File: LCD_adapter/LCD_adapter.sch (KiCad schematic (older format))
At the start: 3 parts, among them U1 RC1602A

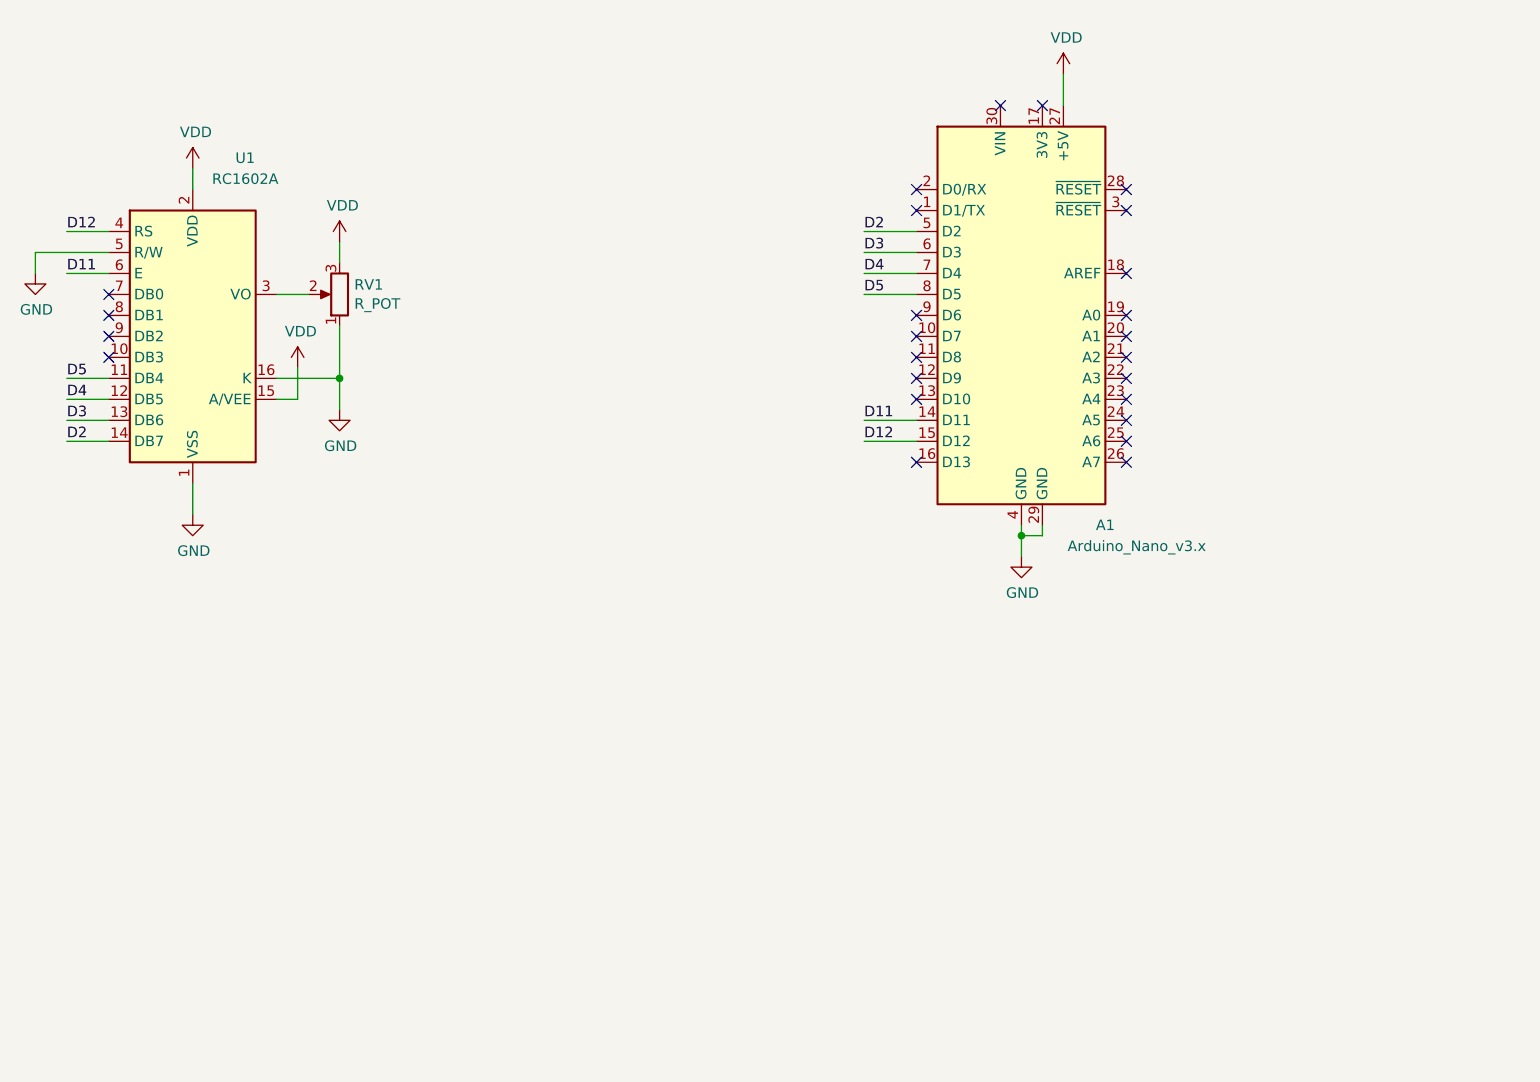
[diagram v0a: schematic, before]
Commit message: bluetooth module v0 - updated to include the bluetooth module and buttons for control
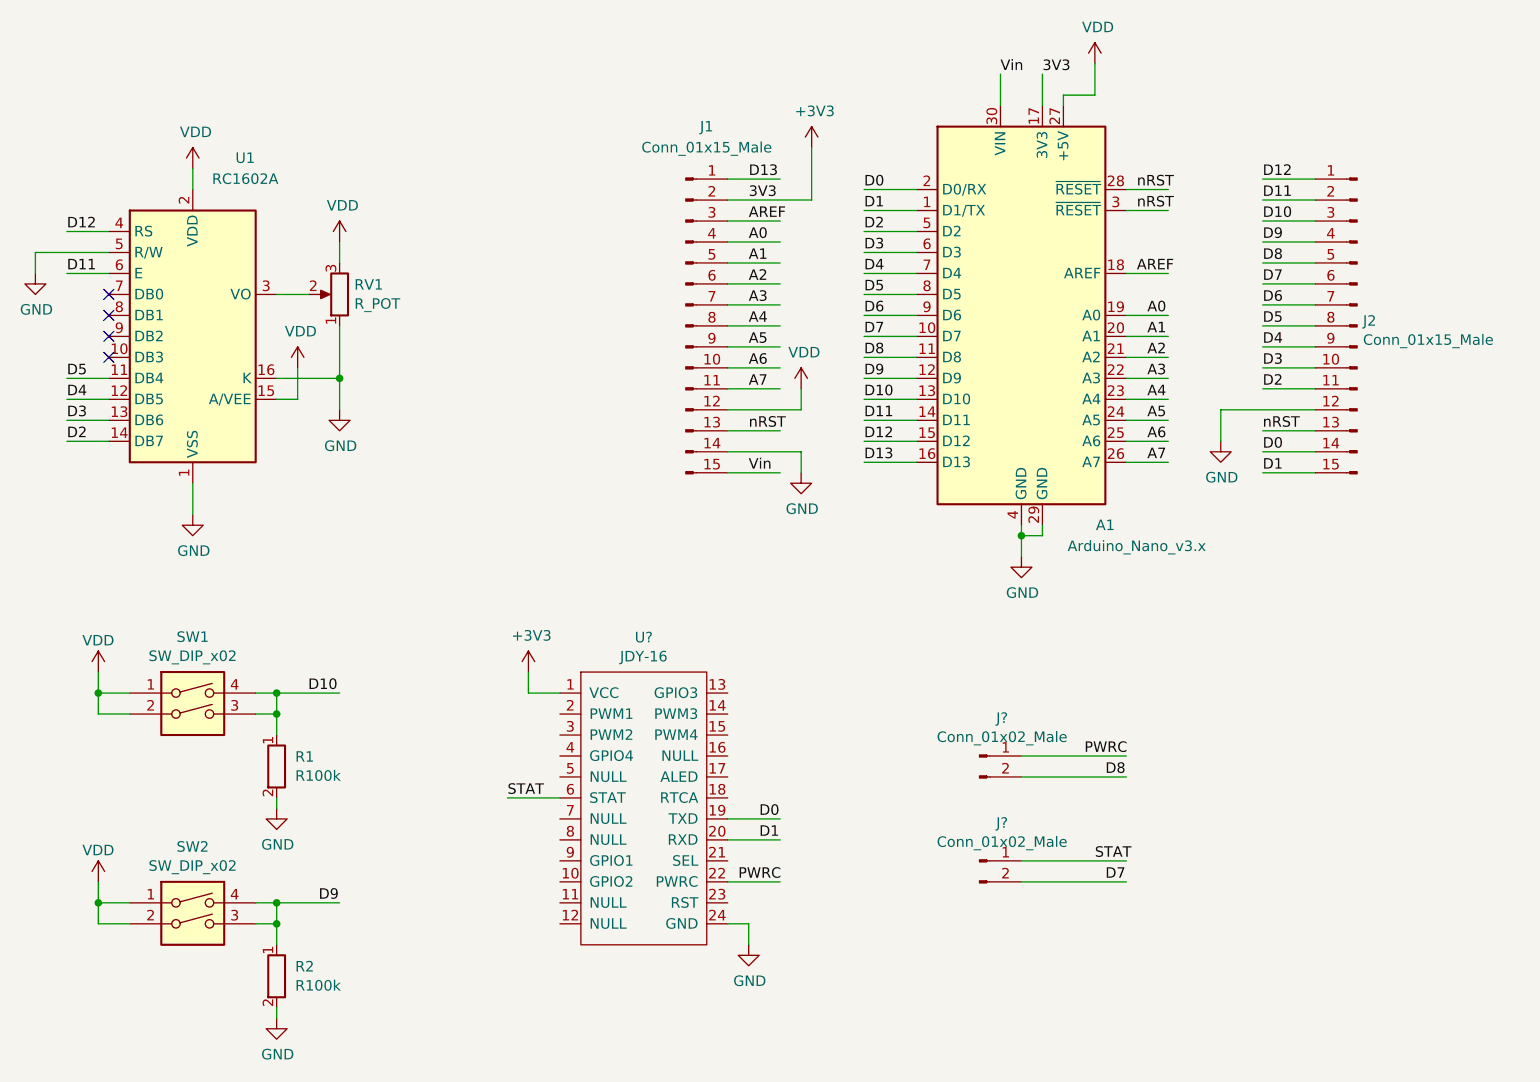
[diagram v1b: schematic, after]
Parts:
- added J1, J2: Conn_01x15_Male, Connector_PinHeader_2.54mm:PinHeader_1x15_P2.54mm_Vertical, symbol Connector:Conn_01x15_Male
- added J? (x2): Conn_01x02_Male, Connector_PinHeader_2.54mm:PinHeader_1x02_P2.54mm_Vertical, symbol Connector:Conn_01x02_Male
- added R1, R2: R100k, Resistor_THT:R_Axial_DIN0207_L6.3mm_D2.5mm_P7.62mm_Horizontal, symbol resistors:R100k
- added SW1, SW2: SW_DIP_x02, brad_footprints:SW_PUSH_6mm_H9.5mm, symbol Switch:SW_DIP_x02
- added U?: JDY-16, brad_footprints:JDY-16, symbol brad_lib:JDY-16
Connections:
- net labels added: +3V3, 3V3, A0, A1, A2, A3, A4, A5, A6, A7, AREF, D0, D1, D10, D13, D6, D7, D8, D9, PWRC, STAT, Vin, nRST
- wire segments 28 -> 117
- no-connect marks 25 -> 4

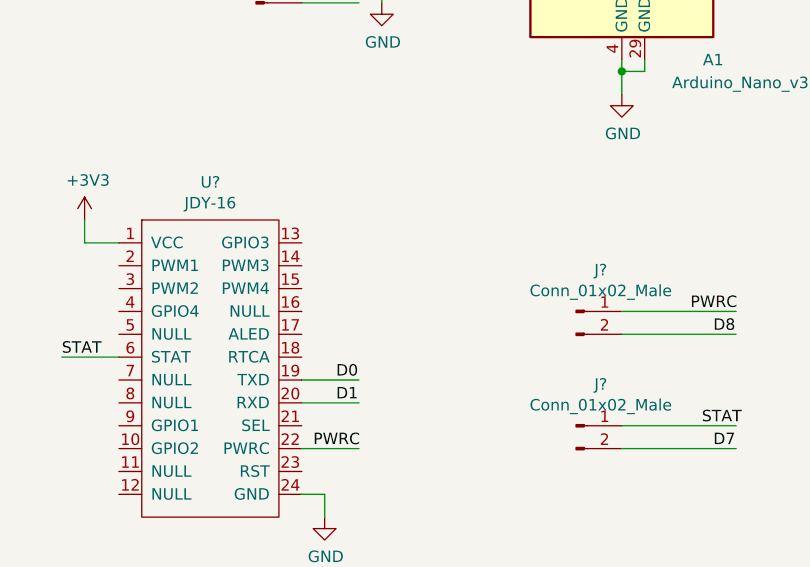
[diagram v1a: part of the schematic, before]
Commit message: fixed for DRC errors
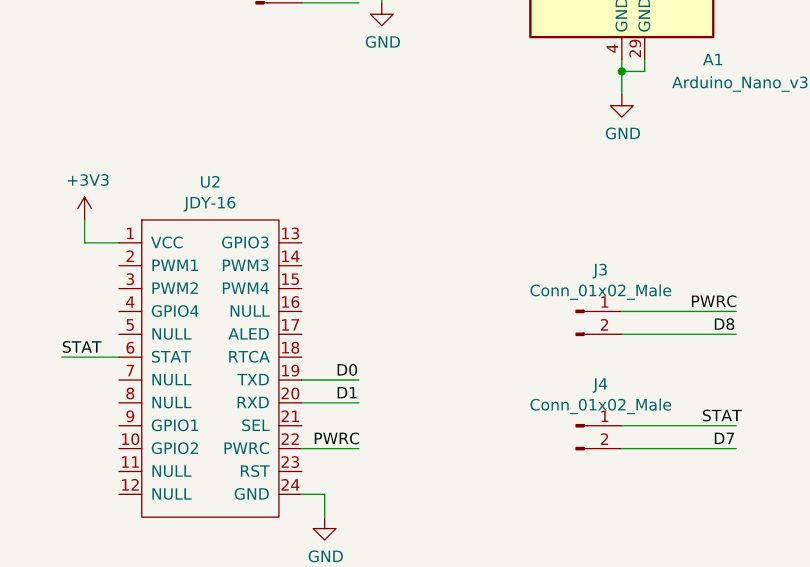
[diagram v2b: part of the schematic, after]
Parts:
- gave numbers to parts that had none: 3
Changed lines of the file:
@@
 D9
 $Comp
-L brad_lib:JDY-16 U?
+L brad_lib:JDY-16 U2
 U 1 1 61DAA5A8
 P 5750 6050
-F 0 "U?" H 5750 6915 50  0000 C CNN
+F 0 "U2" H 5750 6915 50  0000 C CNN
 F 1 "JDY-16" H 5750 6824 50  0000 C CNN
 F 2 "brad_footprints:JDY-16" H 5750 6150 50  0001 C CNN
@@
 $EndComp
 $Comp
-L power:+3V3 #PWR?
+L power:+3V3 #PWR0108
 U 1 1 61DAB957
 P 6550 2850
-F 0 "#PWR?" H 6550 2700 50  0001 C CNN
+F 0 "#PWR0108" H 6550 2700 50  0001 C CNN
 F 1 "+3V3" H 6565 3023 50  0000 C CNN
 F 2 "" H 6550 2850 50  0001 C CNN
@@
 	6150 3100 6550 3100
 $Comp
-L power:+3V3 #PWR?
+L power:+3V3 #PWR0109
 U 1 1 61DB02A3
 P 5200 5350
-F 0 "#PWR?" H 5200 5200 50  0001 C CNN
+F 0 "#PWR0109" H 5200 5200 50  0001 C CNN
 F 1 "+3V3" H 5215 5523 50  0000 C CNN
 F 2 "" H 5200 5350 50  0001 C CNN
@@
 	6250 6550 6250 6650
 $Comp
-L power:GND #PWR?
+L power:GND #PWR0110
 U 1 1 61DCA4E3
 P 6250 6650
-F 0 "#PWR?" H 6250 6400 50  0001 C CNN
+F 0 "#PWR0110" H 6250 6400 50  0001 C CNN
 F 1 "GND" H 6255 6477 50  0000 C CNN
 F 2 "" H 6250 6650 50  0001 C CNN
@@
 D1
 $Comp
-L Connector:Conn_01x02_Male J?
+L Connector:Conn_01x02_Male J3
 U 1 1 61DCACFE
 P 7350 5750
-F 0 "J?" H 7458 5931 50  0000 C CNN
+F 0 "J3" H 7458 5931 50  0000 C CNN
 F 1 "Conn_01x02_Male" H 7458 5840 50  0000 C CNN
 F 2 "Connector_PinHeader_2.54mm:PinHeader_1x02_P2.54mm_Vertical" H 7350 5750 50  0001 C CNN
@@
 $EndComp
 $Comp
-L Connector:Conn_01x02_Male J?
+L Connector:Conn_01x02_Male J4
 U 1 1 61DCBA49
 P 7350 6250
-F 0 "J?" H 7458 6431 50  0000 C CNN
+F 0 "J4" H 7458 6431 50  0000 C CNN
 F 1 "Conn_01x02_Male" H 7458 6340 50  0000 C CNN
 F 2 "Connector_PinHeader_2.54mm:PinHeader_1x02_P2.54mm_Vertical" H 7350 6250 50  0001 C CNN
